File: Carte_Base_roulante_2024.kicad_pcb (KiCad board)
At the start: 2 copper layers, 64 parts, among them J11 ENCA, J4 ENCB, J5 ENCC, Q2 IRF7424, U1 STM32G484RETx

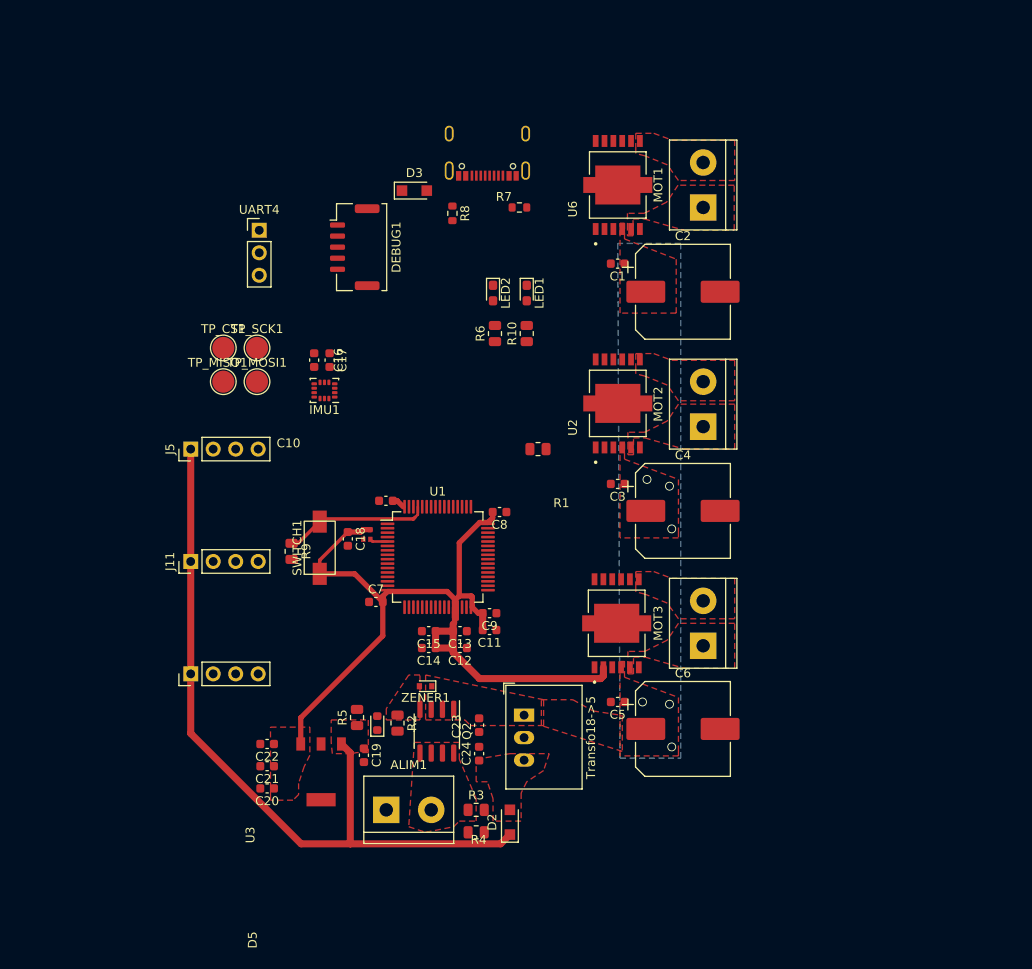
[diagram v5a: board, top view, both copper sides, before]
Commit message: routage avançé
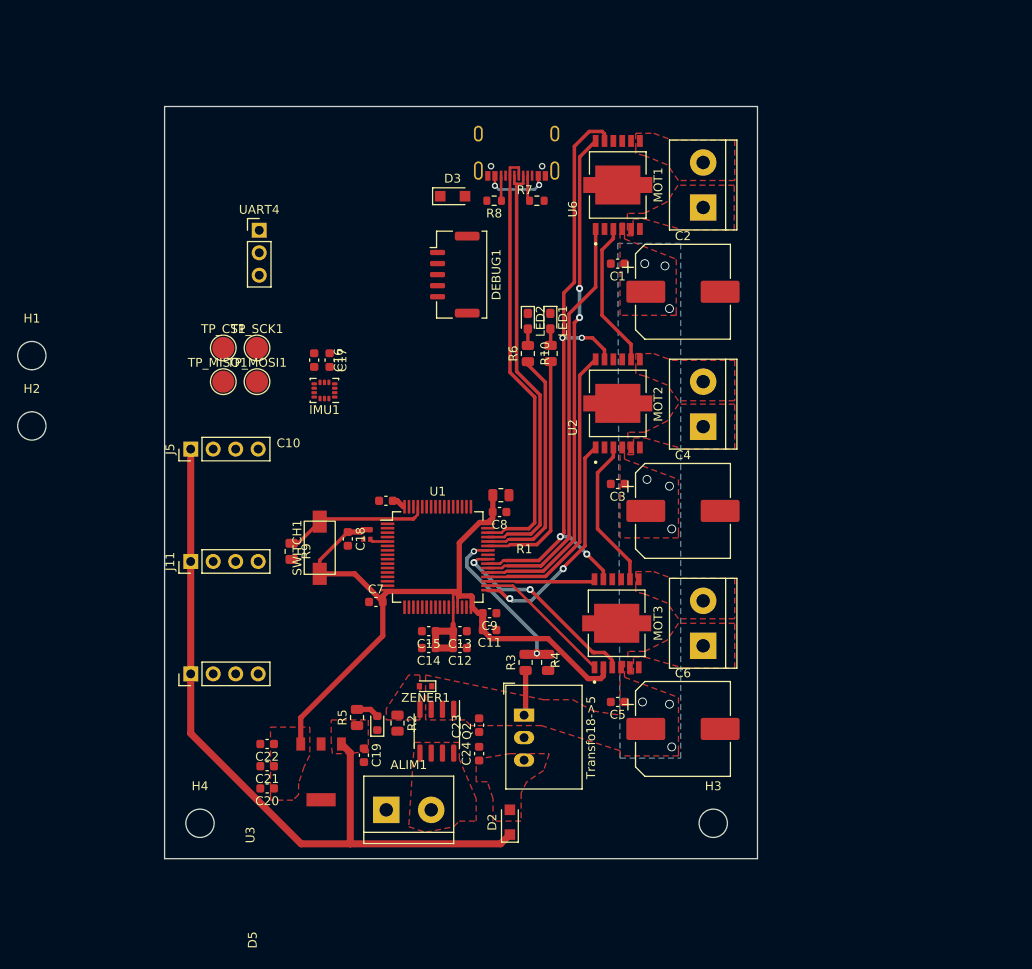
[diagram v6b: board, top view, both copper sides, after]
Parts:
- added H1: MountingHole, MountingHole:MountingHole_3.2mm_M3, F.Cu at (139.0, 80.2)
- added H2: MountingHole, MountingHole:MountingHole_3.2mm_M3, F.Cu at (139.0, 88.2)
- added H3: MountingHole, MountingHole:MountingHole_3.2mm_M3, F.Cu at (216.0, 133.1)
- added H4: MountingHole, MountingHole:MountingHole_3.2mm_M3, F.Cu at (158.0, 133.1)
- moved R4 20.9 mm to (197.4, 114.9), turned to -90 degrees
- moved R3 17.6 mm to (194.8, 114.9), turned to 90 degrees
- moved DEBUG1 11.7 mm to (186.8, 71.1)
- moved R1 6.68 mm to (192.0, 96.0)
- moved LED2 5.06 mm to (195.1, 76.4)
- moved R8 4.93 mm to (191.3, 62.7), turned to 180 degrees
- moved D3 4.37 mm to (186.6, 62.2)
- moved R6 4.35 mm to (195.1, 80.0)
- moved LED1 4.14 mm to (197.6, 76.3)
- moved R10 3.52 mm to (197.6, 80.0)
- moved USB-C1 3.30 mm to (193.8, 55.2)
- moved R7 2.11 mm to (196.1, 62.7)
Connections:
- R3 pad 1: Net-(ALIM1-Pin_2) -> +BATT
- U1 pad 33: DIR3 -> DIR2
- U1 pad 34: DIR2 -> DIR3
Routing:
- net DIS: track 0.00 -> 73.4 mm, vias 0 -> 4
- net PWM1: track 0.00 -> 57.4 mm, vias 0 -> 2
- net USB_DP: track 0.00 -> 49.0 mm
- net USB_DM: track 0.00 -> 48.9 mm
- net DIR1: track 0.00 -> 46.7 mm
- net PWM2: track 0.00 -> 33.4 mm
- net LED1: track 0.00 -> 26.9 mm
- net LED2: track 0.00 -> 26.7 mm
- net DIR2: track 0.00 -> 25.7 mm, vias 0 -> 2
- net ERROR_FLAG: track 0.00 -> 23.0 mm, vias 0 -> 2
- net MEAS_VBAT: track 0.00 -> 19.4 mm, vias 0 -> 2
- net Net-(U2-SO): track 0.00 -> 17.2 mm
- net Net-(U2-SI): track 0.00 -> 16.6 mm
- net DIR3: track 0.00 -> 15.9 mm
- net PWM3: track 0.00 -> 12.2 mm
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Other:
- board outline added: 67 x 85 mm

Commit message: manque plan GNA et pads
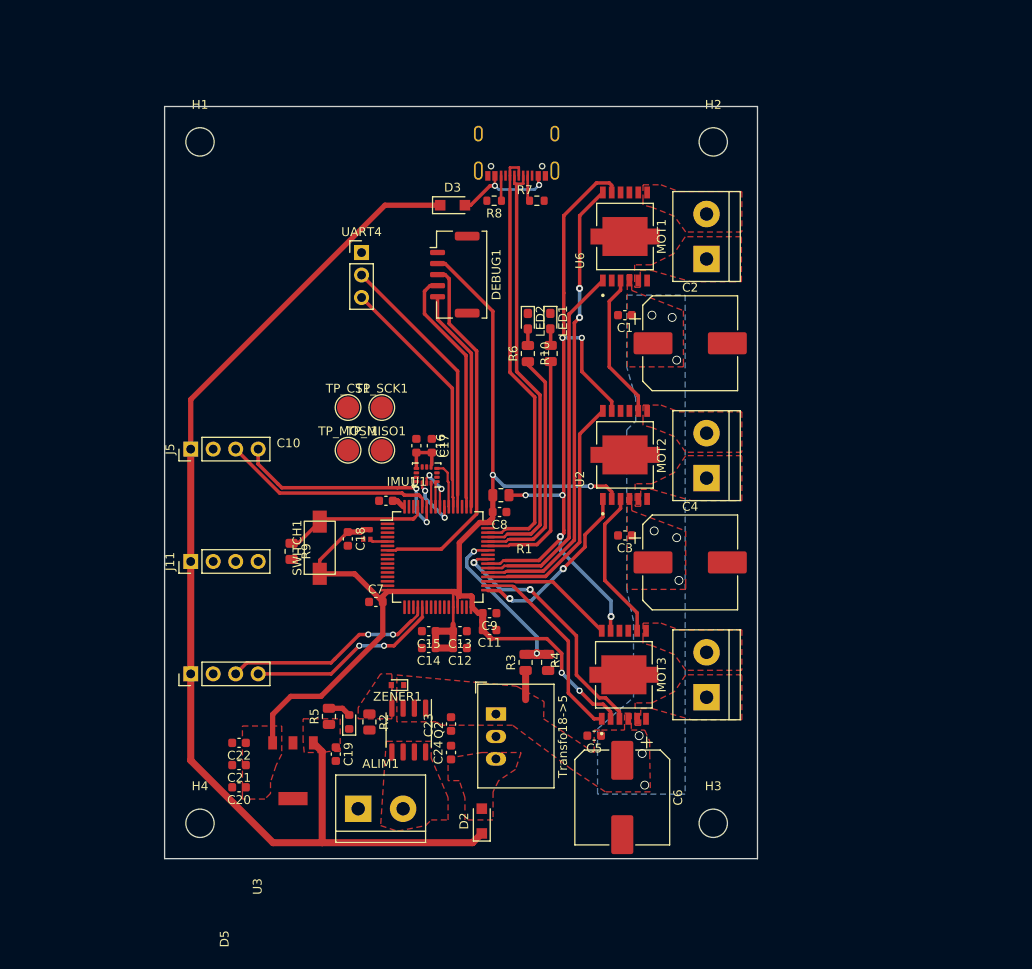
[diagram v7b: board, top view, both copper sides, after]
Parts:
- moved H2 83.4 mm to (216.0, 56.1)
- moved H1 30.7 mm to (158.0, 56.1)
- moved TP_MISO1 19.5 mm to (178.6, 90.9)
- moved TP_CS1 15.6 mm to (174.8, 86.1)
- moved TP_SCK1 15.6 mm to (178.6, 86.1)
- moved C17 15.1 mm to (184.2, 90.4)
- moved C16 15.1 mm to (182.5, 90.4)
- moved IMU1 15.0 mm to (183.6, 93.7)
- moved TP_MOSI1 12.9 mm to (174.8, 90.9)
- moved UART4 11.8 mm to (176.3, 68.6)
- moved C6 10.3 mm to (205.7, 130.2), turned to -90 degrees
- moved C1 5.88 mm to (206.0, 75.7)
- moved U3 5.88 mm to (205.9, 116.3)
- moved U6 5.88 mm to (206.0, 66.8)
- moved C2 5.88 mm to (213.4, 78.8)
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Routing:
- net +3.3V: track 99.1 -> 154.1 mm, vias 0 -> 4
- net +5V: track 85.5 -> 126.9 mm
- net RST: track 0.00 -> 41.1 mm
- net UART4_TX: track 0.00 -> 30.7 mm
- net SWCLK: track 0.00 -> 28.1 mm
- net UART4_RX: track 0.00 -> 27.9 mm
- net Enc3_B: track 0.00 -> 26.7 mm, vias 0 -> 2
- net SWDIO: track 0.00 -> 25.3 mm
- net Enc3_A: track 0.00 -> 24.3 mm
- net Enc2_A: track 0.00 -> 24.2 mm, vias 0 -> 2
- net Enc2_B: track 0.00 -> 23.0 mm, vias 0 -> 2
- net DIS: track 73.4 -> 85.1 mm, vias 4 -> 6
- net DIR3: track 15.9 -> 22.4 mm
- net SPI1_CS_IMU: track 0.00 -> 6.20 mm, vias 0 -> 2
- net ERROR_FLAG: track 23.0 -> 28.6 mm
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
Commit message: almost ended , need GND
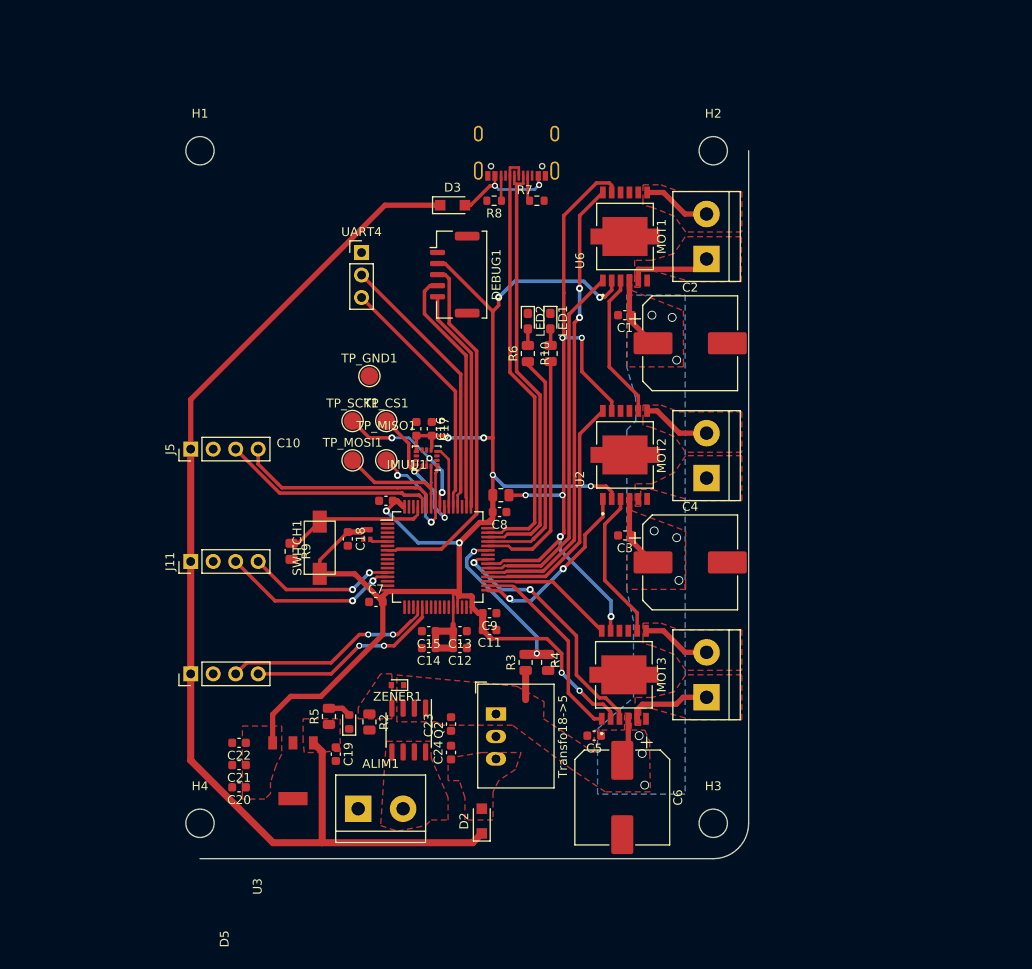
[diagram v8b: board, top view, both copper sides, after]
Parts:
- added TP_GND1: TestPoint, TestPoint:TestPoint_Pad_D2.0mm, F.Cu at (177.2, 82.5)
- TP_CS1, TP_MISO1, TP_MOSI1, TP_SCK1: footprint TestPoint:TestPoint_Pad_D2.5mm -> TestPoint:TestPoint_Pad_D2.0mm
- moved TP_CS1 4.58 mm to (179.1, 87.6)
- moved TP_SCK1 3.64 mm to (175.3, 87.6)
- moved C16 1.91 mm to (182.5, 88.5)
- moved C17 1.91 mm to (184.2, 88.5)
- moved IMU1 1.91 mm to (183.6, 91.8)
- moved TP_MISO1 1.25 mm to (179.1, 92.1)
- moved TP_MOSI1 1.25 mm to (175.3, 92.1)
- moved H1 1.00 mm to (158.0, 57.1)
- moved H2 1.00 mm to (216.0, 57.1)
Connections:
- U1 pad 12: Enc1_A -> Enc1_B
- U1 pad 13: Enc1_B -> Enc1_A
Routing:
- net +3.3V: track 154.1 -> 189.8 mm, vias 4 -> 10
- net +BATT: track 3.55 -> 25.0 mm
- net Enc1_A: track 0.00 -> 20.1 mm, vias 0 -> 2
- net Enc1_B: track 0.00 -> 16.7 mm, vias 0 -> 2
- net SPI1_MISO: track 2.90 -> 16.4 mm, vias 0 -> 2
- net SPI1_SCK: track 5.23 -> 17.6 mm, vias 2 -> 3
- net SPI1_MOSI: track 2.67 -> 14.9 mm
- net SPI1_CS_IMU: track 6.20 -> 16.1 mm
- net Net-(MOT1-Pin_1): track 0.00 -> 9.47 mm
- net Net-(MOT3-Pin_1): track 0.00 -> 9.47 mm
- net Net-(MOT3-Pin_2): track 0.00 -> 7.85 mm
- net Net-(MOT2-Pin_2): track 0.00 -> 7.76 mm
- net Net-(MOT1-Pin_2): track 0.00 -> 7.73 mm
- net Enc3_B: track 26.7 -> 23.5 mm, vias 2 -> 0
- net IMU_INT1: track 5.32 -> 7.10 mm
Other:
- board size 67 x 85 mm -> 62 x 80 mm
